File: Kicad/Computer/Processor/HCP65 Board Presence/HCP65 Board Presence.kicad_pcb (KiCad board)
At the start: 2 copper layers, 18.8 x 33.2 mm, 12 parts, among them IC1 74LVC1G32GV,125, IC2 74LVC574APW,118, IC3 74LVC1G04GV,125, IC5 AP7365-33WG-7, J1 Board 2x12 W15.24mm

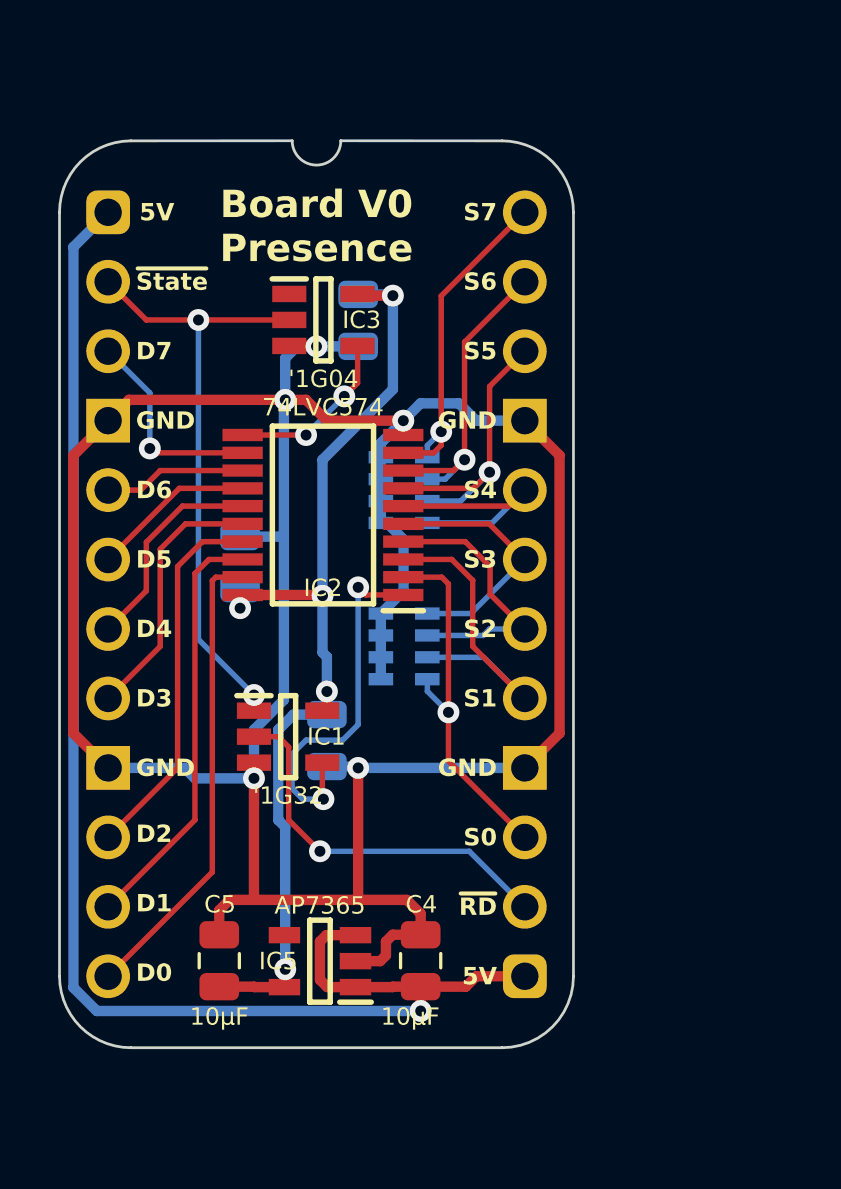
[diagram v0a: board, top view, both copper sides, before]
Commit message: Routed board presence reader on the Processor Board.
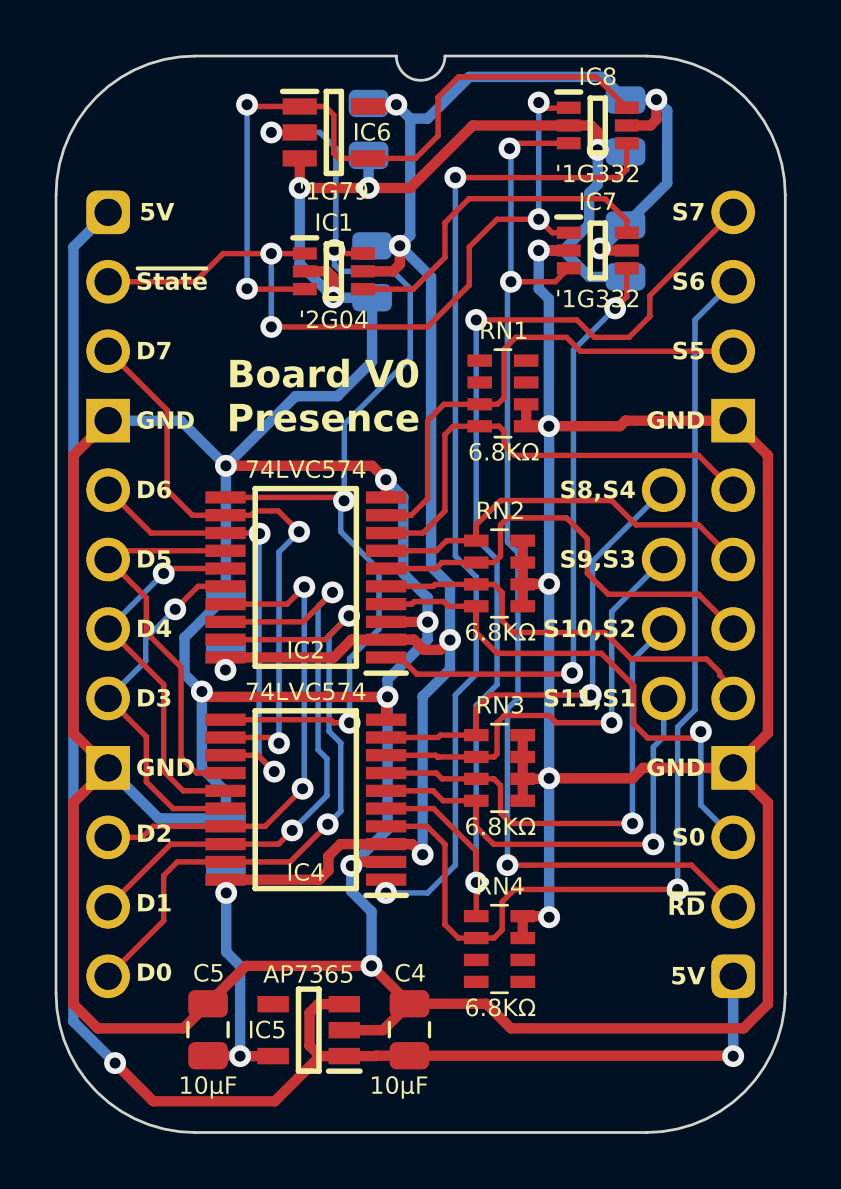
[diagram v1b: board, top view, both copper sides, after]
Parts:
- removed IC3: 74LVC1G04GV,125, SamacSys_Parts:SOT95P275X110-5N
- added C3: 1μF, SamacSys_Parts:C_0805, B.Cu at (4.31, 15.0)
- added C6: 1μF, SamacSys_Parts:C_0805, B.Cu at (4.31, 23.1)
- added C7: 1μF, SamacSys_Parts:C_0805, B.Cu at (9.65, 2.16)
- added IC4: 74LVC574APW,118, SamacSys_Parts:SOP65P640X110-20N, F.Cu at (7.23, 21.5)
- added IC6: 74LVC1G79GV,125, SamacSys_Parts:SOT95P275X110-5N, F.Cu at (8.26, -2.92)
- added IC7: 74LVC1G332GW-Q100H, SamacSys_Parts:SOP65P210X110-6N, F.Cu at (17.9, 1.40)
- added IC8: 74LVC1G332GW-Q100H, SamacSys_Parts:SOP65P210X110-6N, F.Cu at (17.9, -3.17)
- added J3: Conn_01x04_Pin, Connector_PinHeader_2.54mm:PinHeader_1x04_P2.54mm_Vertical, B.Cu at (20.3, 10.2)
- added RN3: CAY16-682J4LF, SamacSys_Parts:CAY16-J4, F.Cu at (14.3, 20.3)
- added RN4: CAY16-682J4LF, SamacSys_Parts:CAY16-J4, F.Cu at (14.3, 26.9)
- IC1: value 74LVC1G32GV,125 -> 74LVC2G04GW-Q100H; footprint SamacSys_Parts:SOT95P275X110-5N -> SamacSys_Parts:SOP65P210X110-6N
- J1: value Board 2x12 W15.24mm -> Board 2x12 W22.86mm; footprint SamacSys_Parts:DIP-24_Board_W15.24mm -> SamacSys_Parts:DIP-24_Board_W22.86mm
- RN1, RN2: moved to F.Cu
- moved C1 21.0 mm to (18.9, 1.40)
- moved IC1 17.1 mm to (8.26, 2.16)
- moved C9 16.6 mm to (9.53, -3.05), turned to 0 degrees
- moved C2 12.1 mm to (18.9, -3.17)
- moved RN1 5.10 mm to (14.5, 6.62), turned to 180 degrees
- moved RN2 4.44 mm to (14.3, 13.2), turned to 180 degrees
- moved C4 2.56 mm to (11.0, 29.9)
- moved C5 2.56 mm to (3.65, 29.9)
- moved IC5 2.56 mm to (7.34, 29.9)
- moved IC2 2.37 mm to (7.23, 13.4)
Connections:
- net ~{Read State} renamed ~{State}
- IC1 pad 2: ~{RD} -> GND
- IC1 pad 3: GND -> /Q
- IC1 pad 4: /~{Read State+RD} -> /~{Q}
- IC2 pad 1: /~{Read State+RD} -> /~{Read State}0
- IC2 pad 11: /Read State -> /State
- IC2 pad 2: S0 -> /3.3V
- IC2 pad 3: S1 -> GND
- IC2 pad 4: S2 -> S0
- IC2 pad 5: S3 -> S1
- IC2 pad 6: S4 -> S2
- IC2 pad 7: S5 -> S3
- IC2 pad 8: S6 -> S4
- IC2 pad 9: S7 -> S5
- RN1 pad 1: S7 -> unconnected-(RN1-R1-Pad1)
- RN1 pad 2: S6 -> unconnected-(RN1-R2-Pad2)
- RN1 pad 7: GND -> unconnected-(RN1-R2-Pad7)
- RN1 pad 8: GND -> unconnected-(RN1-R1-Pad8)
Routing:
- net GND: track 110.6 -> 228.3 mm, vias 5 -> 16
- net /3.3V: track 37.8 -> 81.9 mm, vias 5 -> 9
- net /State: track 0.00 -> 39.1 mm, vias 0 -> 4
- net /~{Read State}1: track 0.00 -> 36.6 mm, vias 0 -> 2
- net S7: track 12.4 -> 39.5 mm, vias 1 -> 2
- net S6: track 11.5 -> 38.5 mm
- net /Q: track 0.00 -> 26.9 mm, vias 0 -> 2
- net ~{RD}: track 14.0 -> 40.0 mm, vias 1 -> 3
- net /~{Read State}0: track 0.00 -> 22.2 mm, vias 0 -> 2
- net S9: track 0.00 -> 18.0 mm, vias 0 -> 1
- net S11: track 0.00 -> 17.3 mm, vias 0 -> 1
- net S8: track 0.00 -> 16.6 mm, vias 0 -> 1
- net S10: track 0.00 -> 16.5 mm, vias 0 -> 1
- net D7: track 7.65 -> 21.6 mm, vias 1 -> 2
- net /~{Read State+RD}: track 13.6 -> 0.00 mm, vias 2 -> 0
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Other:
- board size 18.8 x 33.2 mm -> 26.7 x 39.4 mm
- board text added: "S10,S2"
- board text added: "S11,S1"
- board text added: "S8,S4"
- board text added: "S9,S3"
- board text removed: "S1"
- board text removed: "S2"
- board text removed: "S3"
- board text removed: "S4"
